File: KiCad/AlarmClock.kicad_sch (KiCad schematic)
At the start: 75 parts, among them SW1 RotaryEncoder_Switch, SW2 SW_SPST, SW3 SW_Push, U1 D168K, U10 TPIC6595, U11 TPIC6595, U12 TPIC6595, U13 TPIC6595, U14 TPIC6595, U15 TPIC6595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

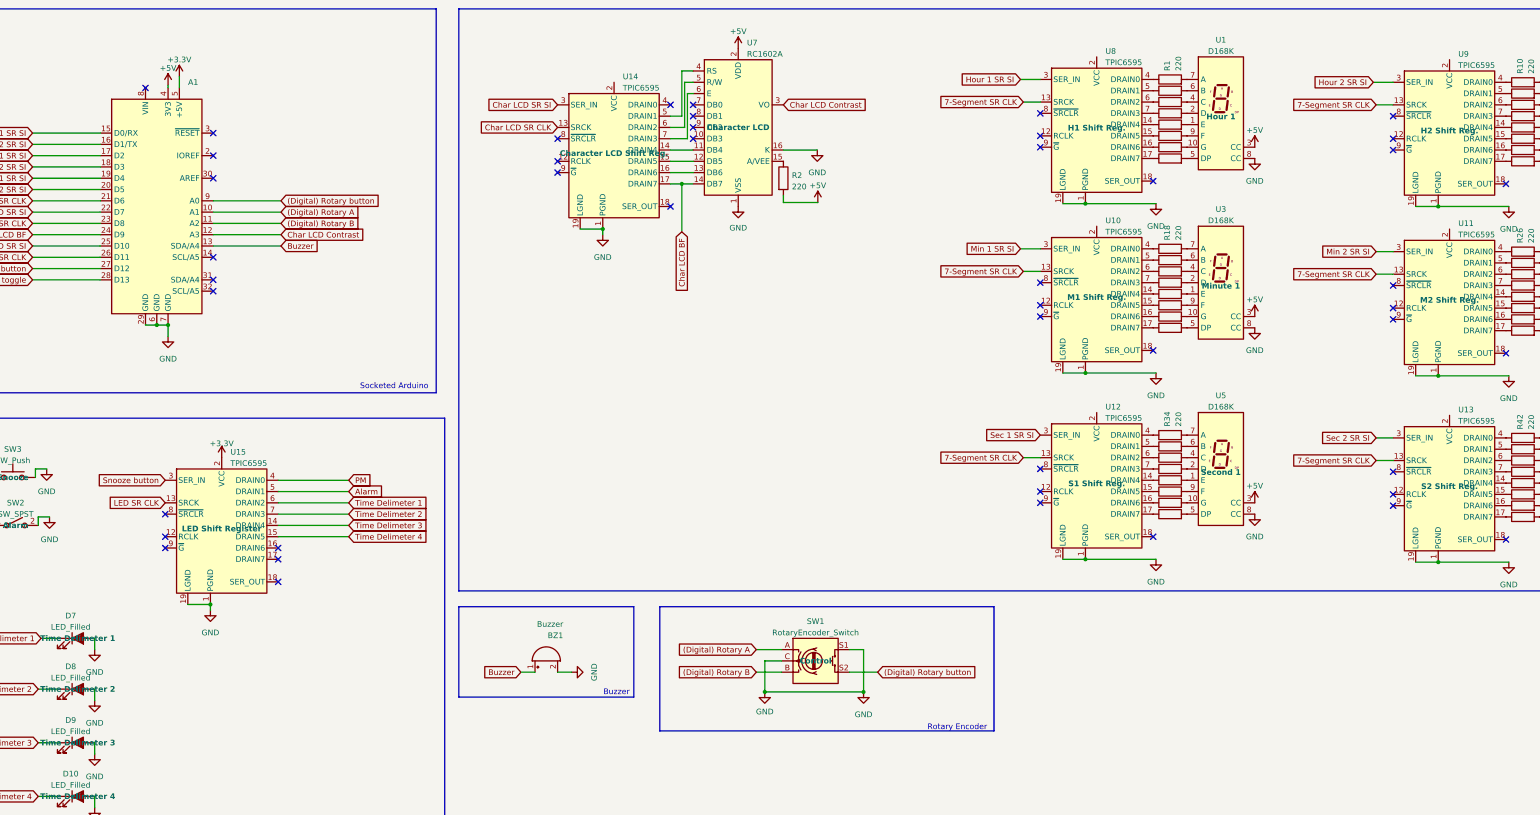
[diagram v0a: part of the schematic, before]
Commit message: Update schematic to adhere to ERC
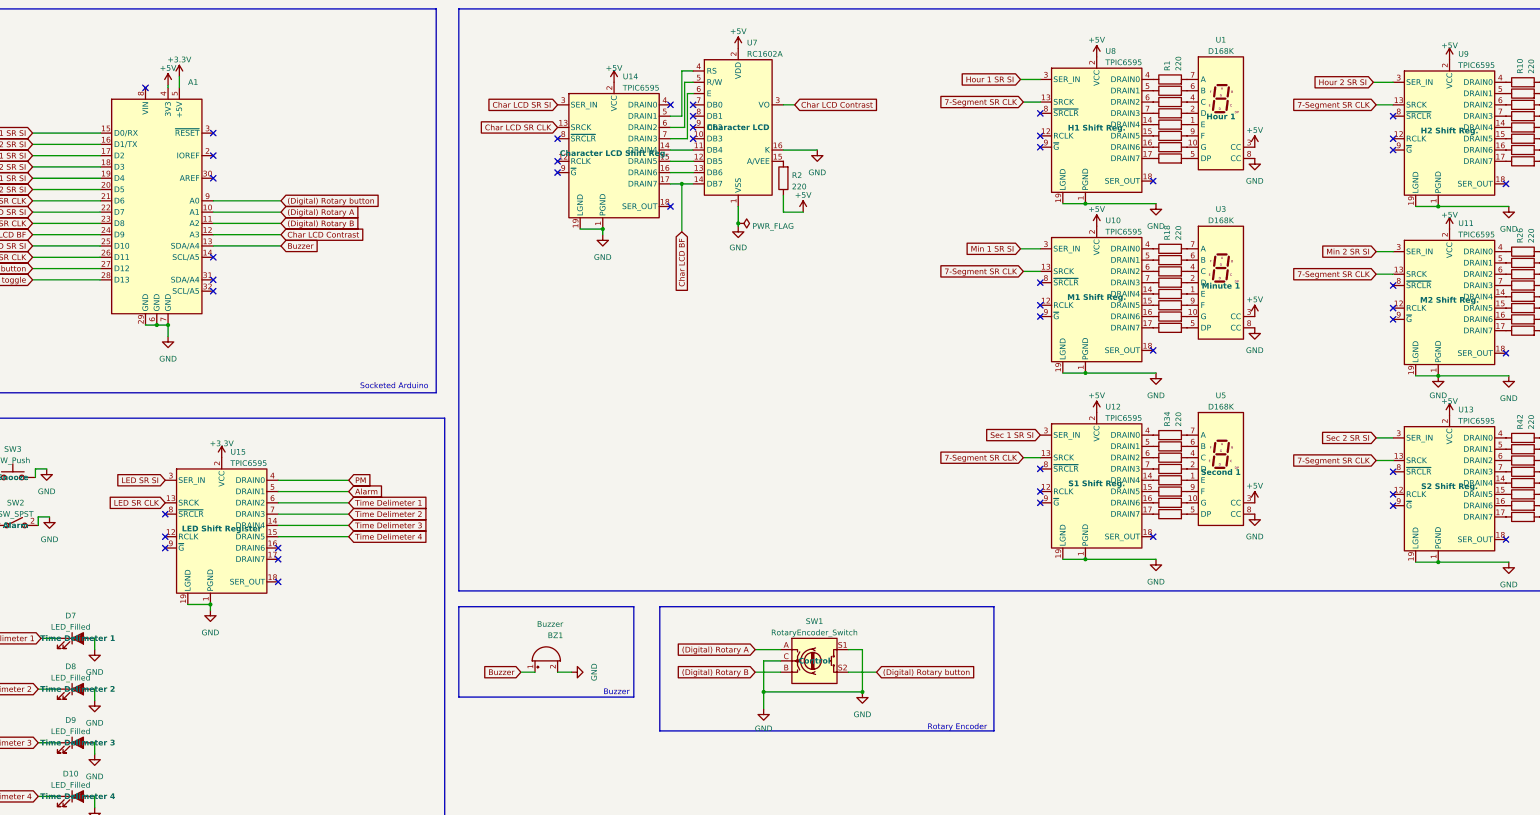
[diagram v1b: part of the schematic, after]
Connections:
- net +5V: now also R2.1, U10.2 (VCC), U11.2 (VCC), U12.2 (VCC), U13.2 (VCC), U14.2 (VCC), U8.2 (VCC), U9.2 (VCC); no longer R2.2
- net LED SR SI: now also U15.3 (SER_IN)
- net Snooze button: no longer U15.3 (SER_IN)
- net at U7.15 (A/VEE): now also R2.2; no longer R2.1
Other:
- moved on the sheet: R2
